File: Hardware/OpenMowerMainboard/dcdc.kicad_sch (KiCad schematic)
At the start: 23 parts, among them IC3 MAX20405AFOF_VY+T

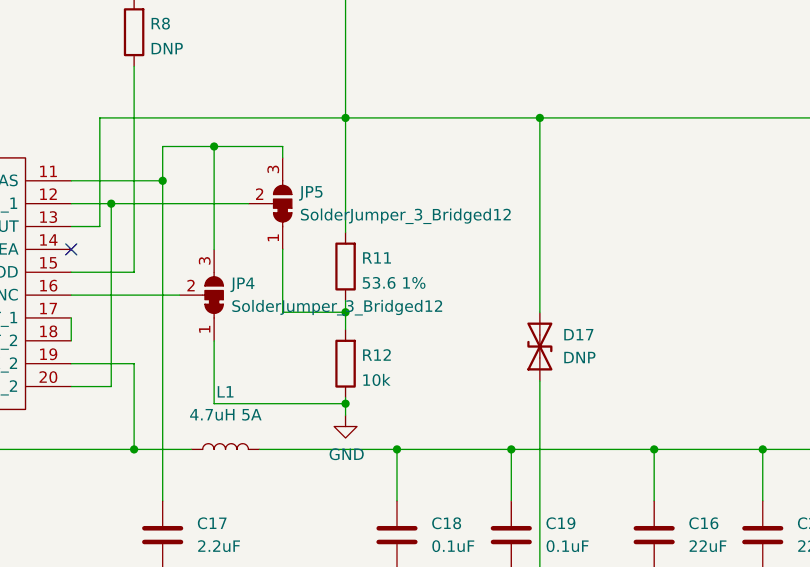
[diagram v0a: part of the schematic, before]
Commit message: fix: R11 notation 53k6
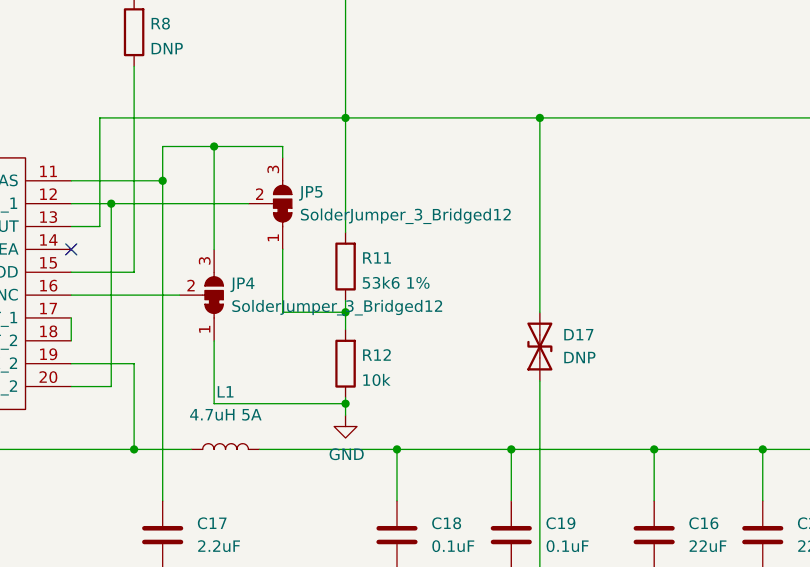
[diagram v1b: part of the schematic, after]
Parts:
- R11: value 53.6 1% -> 53k6 1%
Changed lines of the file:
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@@
       (effects (font (size 1.27 1.27)) (justify right))
     )
-    (property "Value" "53.6 1%" (id 1) (at 166.878 108.5466 0)
+    (property "Value" "53k6 1%" (id 1) (at 166.878 108.5466 0)
       (effects (font (size 1.27 1.27)) (justify right))
     )

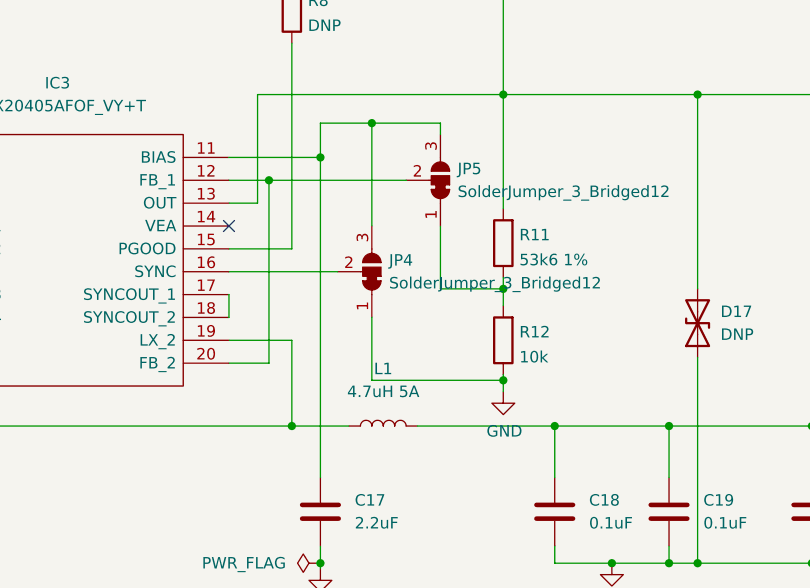
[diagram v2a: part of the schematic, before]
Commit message: feat: update to Kicad7, put back C2,C3
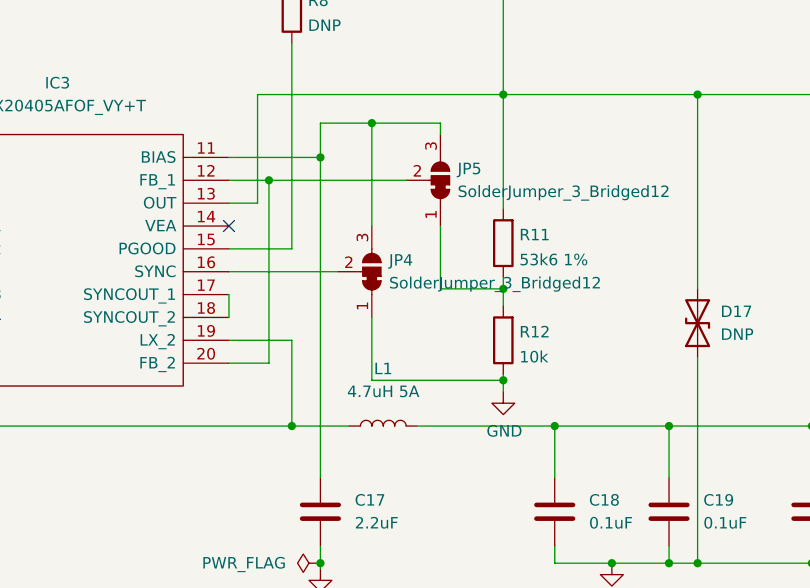
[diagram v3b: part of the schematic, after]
